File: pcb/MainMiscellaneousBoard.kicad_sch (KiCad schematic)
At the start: 1 part

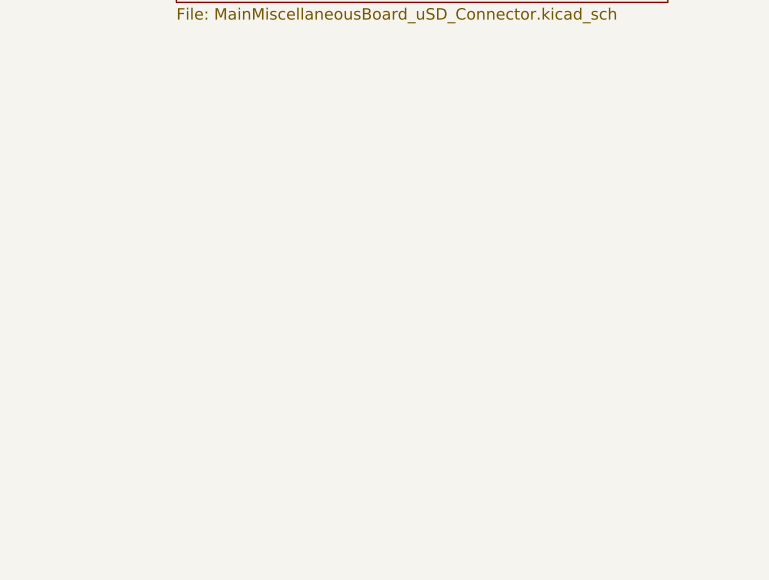
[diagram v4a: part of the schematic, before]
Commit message: Made symbol for ItsyBitsy ESP32.
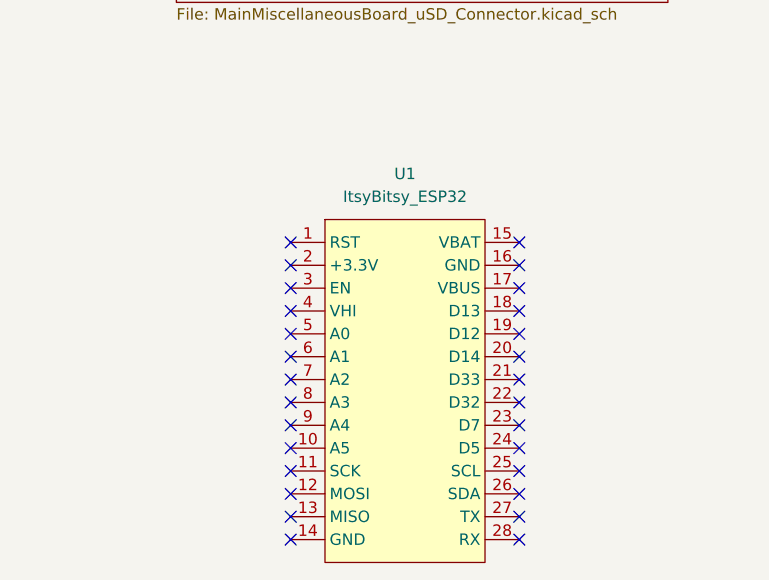
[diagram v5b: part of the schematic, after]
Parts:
- added U1: ItsyBitsy_ESP32, pcb:ItsyBitsy_ESP32, symbol ItsyBitsy_ESP32:ItsyBitsy_ESP32
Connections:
- no-connect marks 102 -> 130
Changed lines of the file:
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@@
 	(paper "A2")
 	(no_connect
+		(at 488.95 358.14)
+	)
+	(no_connect
+		(at 488.95 342.9)
+	)
+	(no_connect
 		(at 468.63 133.35)
 	)
@@
 	)
 	(no_connect
+		(at 514.35 340.36)
+	)
+	(no_connect
 		(at 468.63 166.37)
 	)
@@
 	)
 	(no_connect
+		(at 488.95 335.28)
+	)
+	(no_connect
 		(at 468.63 163.83)
 	)
@@
 	)
 	(no_connect
+		(at 514.35 353.06)
+	)
+	(no_connect
 		(at 468.63 105.41)
 	)
@@
 	)
 	(no_connect
+		(at 514.35 363.22)
+	)
+	(no_connect
+		(at 514.35 332.74)
+	)
+	(no_connect
 		(at 468.63 173.99)
 	)
@@
 	)
 	(no_connect
+		(at 514.35 350.52)
+	)
+	(no_connect
 		(at 468.63 143.51)
 	)
@@
 	)
 	(no_connect
+		(at 488.95 332.74)
+	)
+	(no_connect
 		(at 468.63 123.19)
 	)
@@
 	)
 	(no_connect
+		(at 514.35 355.6)
+	)
+	(no_connect
 		(at 468.63 72.39)
 	)
 	(no_connect
+		(at 514.35 345.44)
+	)
+	(no_connect
 		(at 468.63 87.63)
 	)
@@
 	)
 	(no_connect
+		(at 488.95 365.76)
+	)
+	(no_connect
 		(at 468.63 92.71)
 	)
@@
 	)
 	(no_connect
+		(at 514.35 335.28)
+	)
+	(no_connect
 		(at 537.21 125.73)
 	)
 	(no_connect
+		(at 488.95 353.06)
+	)
+	(no_connect
 		(at 537.21 82.55)
 	)
@@
 	)
 	(no_connect
+		(at 488.95 340.36)
+	)
+	(no_connect
+		(at 488.95 345.44)
+	)
+	(no_connect
 		(at 537.21 113.03)
 	)
 	(no_connect
+		(at 514.35 347.98)
+	)
+	(no_connect
 		(at 537.21 138.43)
 	)
@@
 	)
 	(no_connect
+		(at 514.35 358.14)
+	)
+	(no_connect
 		(at 468.63 77.47)
 	)
 	(no_connect
+		(at 514.35 342.9)
+	)
+	(no_connect
 		(at 468.63 85.09)
 	)
@@
 	)
 	(no_connect
+		(at 488.95 337.82)
+	)
+	(no_connect
 		(at 468.63 110.49)
 	)
@@
 	)
 	(no_connect
+		(at 514.35 337.82)
+	)
+	(no_connect
+		(at 488.95 363.22)
+	)
+	(no_connect
 		(at 537.21 95.25)
 	)
@@
 	)
 	(no_connect
+		(at 514.35 360.68)
+	)
+	(no_connect
+		(at 488.95 355.6)
+	)
+	(no_connect
 		(at 468.63 80.01)
 	)
@@
 	)
 	(no_connect
+		(at 488.95 350.52)
+	)
+	(no_connect
+		(at 514.35 365.76)
+	)
+	(no_connect
 		(at 537.21 156.21)
 	)
@@
 	)
 	(no_connect
+		(at 488.95 360.68)
+	)
+	(no_connect
 		(at 468.63 171.45)
 	)
@@
 	(no_connect
 		(at 537.21 118.11)
+	)
+	(no_connect
+		(at 488.95 347.98)
 	)
 	(no_connect
@@
 					(unit 1)
 				)
+			)
+		)
+	)
+	(symbol
+		(lib_id "ItsyBitsy_ESP32:ItsyBitsy_ESP32")
+		(at 501.65 330.2 0)
+		(unit 1)
+		(exclude_from_sim no)
+		(in_bom yes)
+		(on_board yes)
+		(dnp no)
+		(fields_autoplaced yes)
+		(property "Reference" "U1"
+			(at 501.65 325.12 0)
+			(effects
+				(font
+					(size 1.27 1.27)
+				)
+			)
+		)
+		(property "Value" "ItsyBitsy_ESP32"
+			(at 501.65 327.66 0)
+			(effects
+				(font
+					(size 1.27 1.27)
+				)
+			)
+		)
+		(property "Footprint" "pcb:ItsyBitsy_ESP32"
+			(at 501.65 330.2 0)
+			(effects
+				(font
+					(size 1.27 1.27)
+				)
+				(hide yes)
+			)
+		)
+		(property "Datasheet" ""
+			(at 501.65 330.2 0)
+			(effects
+				(font
+					(size 1.27 1.27)
+				)
+				(hide yes)
+			)
+		)
+		(property "Description" ""
+			(at 501.65 330.2 0)
+			(effects
+				(font
+					(size 1.27 1.27)
+				)
+				(hide yes)
+			)
+		)
+		(pin "1"
+		)
+		(pin "13"
+		)
+		(pin "7"
+		)
+		(pin "2"
+		)
+		(pin "6"
+		)
+		(pin "20"
+		)
+		(pin "4"
+		)
+		(pin "8"
+		)
+		(pin "10"
+		)
+		(pin "11"
+		)
+		(pin "3"
+		)
+		(pin "5"
+		)
+		(pin "9"
+		)
+		(pin "12"
+		)
+		(pin "15"
+		)
+		(pin "17"
+		)
+		(pin "18"
+		)
+		(pin "14"
+		)
+		(pin "16"
+		)
+		(pin "19"
+		)
+		(pin "24"
+		)
+		(pin "28"
+		)
+		(pin "21"
+		)
+		(pin "25"
+		)
+		(pin "26"
+		)
+		(pin "22"
+		)
+		(pin "27"
+		)
+		(pin "23"
+		)
+		(instances
+			(project ""
+				(path "/98fc9565-7d66-4cd3-b0d6-fc60566bea9b"
+					(reference "U1")
+					(unit 1)
+				)

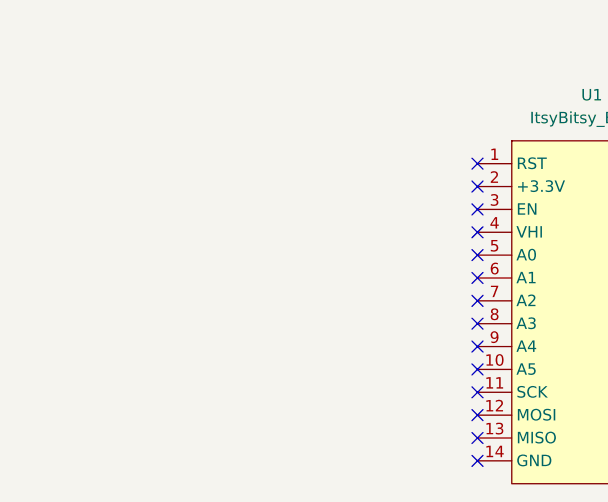
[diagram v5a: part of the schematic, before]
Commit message: Made SEEED Studio XIAO ESP32-S3 Sense symbol and footprint.
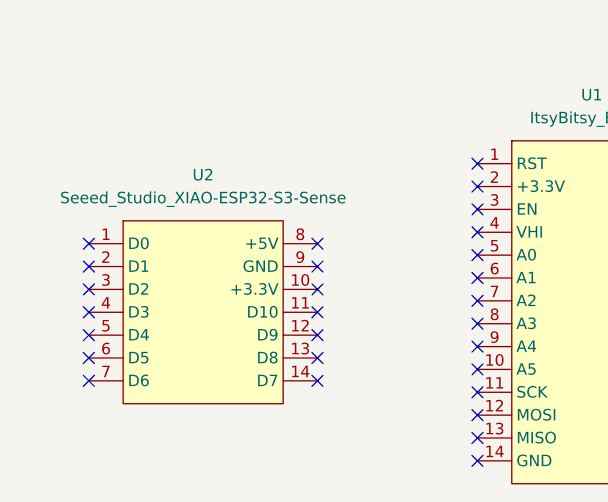
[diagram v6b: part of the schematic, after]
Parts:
- added U2: Seeed_Studio_XIAO-ESP32-S3-Sense, pcb:Seeed_Studio_XIAO_ESP32_S3, symbol Seeed_Studio_XIAO-ESP32-S3-Sense:Seeed_Studio_XIAO-ESP32-S3-Sense
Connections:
- no-connect marks 130 -> 144
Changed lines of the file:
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@@
 	(paper "A2")
 	(no_connect
+		(at 445.77 356.87)
+	)
+	(no_connect
 		(at 488.95 358.14)
 	)
@@
 	)
 	(no_connect
+		(at 471.17 346.71)
+	)
+	(no_connect
 		(at 468.63 166.37)
 	)
@@
 	)
 	(no_connect
+		(at 471.17 351.79)
+	)
+	(no_connect
 		(at 537.21 176.53)
 	)
@@
 	)
 	(no_connect
+		(at 471.17 341.63)
+	)
+	(no_connect
 		(at 468.63 95.25)
 	)
@@
 	)
 	(no_connect
+		(at 445.77 349.25)
+	)
+	(no_connect
 		(at 468.63 113.03)
 	)
@@
 	)
 	(no_connect
+		(at 445.77 341.63)
+	)
+	(no_connect
 		(at 468.63 128.27)
 	)
@@
 	)
 	(no_connect
+		(at 471.17 349.25)
+	)
+	(no_connect
 		(at 537.21 52.07)
 	)
 	(no_connect
+		(at 445.77 354.33)
+	)
+	(no_connect
 		(at 468.63 57.15)
 	)
@@
 	)
 	(no_connect
+		(at 445.77 351.79)
+	)
+	(no_connect
 		(at 537.21 82.55)
 	)
@@
 	)
 	(no_connect
+		(at 445.77 346.71)
+	)
+	(no_connect
 		(at 537.21 181.61)
 	)
@@
 	)
 	(no_connect
+		(at 445.77 344.17)
+	)
+	(no_connect
+		(at 471.17 356.87)
+	)
+	(no_connect
 		(at 488.95 345.44)
 	)
 	(no_connect
+		(at 471.17 344.17)
+	)
+	(no_connect
 		(at 537.21 113.03)
 	)
@@
 	(no_connect
 		(at 468.63 171.45)
+	)
+	(no_connect
+		(at 471.17 354.33)
 	)
 	(no_connect
@@
 					(unit 1)
 				)
+			)
+		)
+	)
+	(symbol
+		(lib_id "Seeed_Studio_XIAO-ESP32-S3-Sense:Seeed_Studio_XIAO-ESP32-S3-Sense")
+		(at 458.47 339.09 0)
+		(unit 1)
+		(exclude_from_sim no)
+		(in_bom yes)
+		(on_board yes)
+		(dnp no)
+		(fields_autoplaced yes)
+		(property "Reference" "U2"
+			(at 458.47 334.01 0)
+			(effects
+				(font
+					(size 1.27 1.27)
+				)
+			)
+		)
+		(property "Value" "Seeed_Studio_XIAO-ESP32-S3-Sense"
+			(at 458.47 336.55 0)
+			(effects
+				(font
+					(size 1.27 1.27)
+				)
+			)
+		)
+		(property "Footprint" "pcb:Seeed_Studio_XIAO_ESP32_S3"
+			(at 458.47 339.09 0)
+			(effects
+				(font
+					(size 1.27 1.27)
+				)
+				(hide yes)
+			)
+		)
+		(property "Datasheet" ""
+			(at 458.47 339.09 0)
+			(effects
+				(font
+					(size 1.27 1.27)
+				)
+				(hide yes)
+			)
+		)
+		(property "Description" ""
+			(at 458.47 339.09 0)
+			(effects
+				(font
+					(size 1.27 1.27)
+				)
+				(hide yes)
+			)
+		)
+		(pin "6"
+		)
+		(pin "13"
+		)
+		(pin "4"
+		)
+		(pin "9"
+		)
+		(pin "7"
+		)
+		(pin "5"
+		)
+		(pin "11"
+		)
+		(pin "8"
+		)
+		(pin "3"
+		)
+		(pin "10"
+		)
+		(pin "2"
+		)
+		(pin "1"
+		)
+		(pin "12"
+		)
+		(pin "14"
+		)
+		(instances
+			(project "MainMiscellaneousBoard"
+				(path "/98fc9565-7d66-4cd3-b0d6-fc60566bea9b"
+					(reference "U2")
+					(unit 1)
+				)

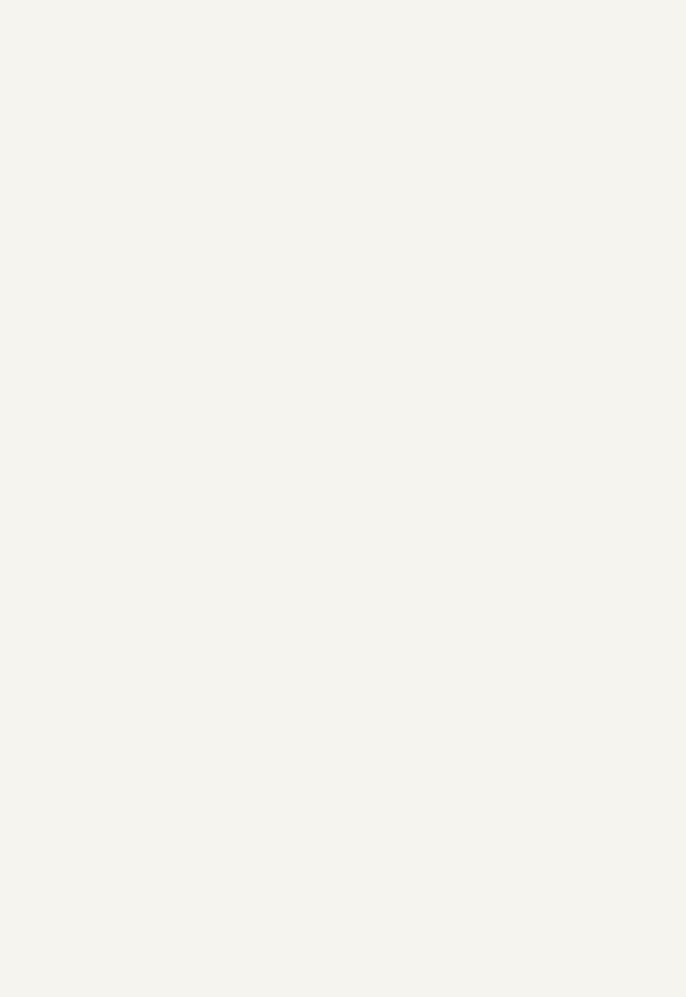
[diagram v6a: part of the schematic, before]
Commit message: Added in some miscellaneous connectors.
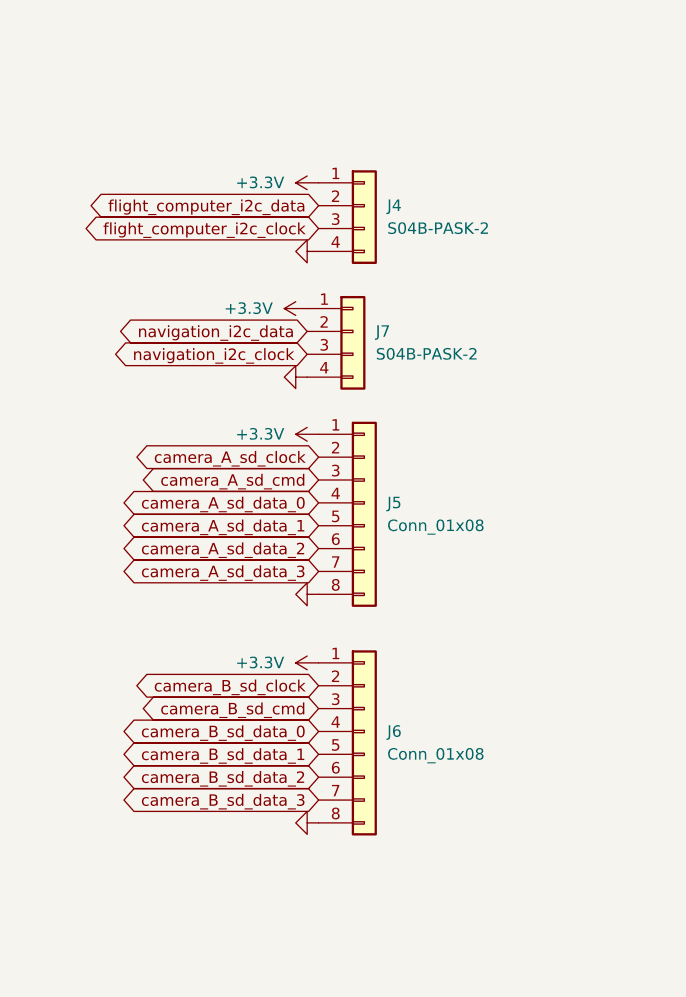
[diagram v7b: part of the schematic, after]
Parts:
- added J4, J7: S04B-PASK-2, pcb:S04B-PASK-2, symbol Connector_Generic:Conn_01x04
- added J5, J6: Conn_01x08, symbol Connector_Generic:Conn_01x08
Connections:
- net camera_A_sd_clock: now also J5.2 (Pin_2)
- net camera_A_sd_cmd: now also J5.3 (Pin_3)
- net camera_A_sd_data_0: now also J5.4 (Pin_4)
- net camera_A_sd_data_1: now also J5.5 (Pin_5)
- net camera_A_sd_data_2: now also J5.6 (Pin_6)
- net camera_A_sd_data_3: now also J5.7 (Pin_7)
- net camera_B_sd_clock: now also J6.2 (Pin_2)
- net camera_B_sd_cmd: now also J6.3 (Pin_3)
- net camera_B_sd_data_0: now also J6.4 (Pin_4)
- net camera_B_sd_data_1: now also J6.5 (Pin_5)
- net camera_B_sd_data_2: now also J6.6 (Pin_6)
- net camera_B_sd_data_3: now also J6.7 (Pin_7)
- new net +3.3V: J4.1 (Pin_1), J5.1 (Pin_1), J6.1 (Pin_1), J7.1 (Pin_1)
- new net GND: J4.4 (Pin_4), J5.8 (Pin_8), J6.8 (Pin_8), J7.4 (Pin_4)
- new net flight_computer_i2c_clock: J4.3 (Pin_3)
- new net flight_computer_i2c_data: J4.2 (Pin_2)
- new net navigation_i2c_clock: J7.3 (Pin_3)
- new net navigation_i2c_data: J7.2 (Pin_2)

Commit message: Added edge connector for `MainMiscellaneousBoard`.
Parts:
- removed J4, J7: S04B-PASK-2, pcb:S04B-PASK-2, symbol Connector_Generic:Conn_01x04
- removed J5, J6: Conn_01x08, symbol Connector_Generic:Conn_01x08
- added J8: PREC040DBAN-M71RC, Connector_PinHeader_2.54mm:PinHeader_2x16_P2.54mm_Horizontal, symbol Connector_Generic:Conn_02x16_Odd_Even
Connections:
- net +3.3V: now also J8.1 (Pin_1), J8.17 (Pin_17), J8.2 (Pin_2), J8.9 (Pin_9)
- net GND: now also J8.15 (Pin_15), J8.16 (Pin_16), J8.31 (Pin_31), J8.7 (Pin_7)
- net camera_A_sd_clock: now also J8.19 (Pin_19)
- net camera_A_sd_cmd: now also J8.21 (Pin_21)
- net camera_A_sd_data_0: now also J8.23 (Pin_23)
- net camera_A_sd_data_1: now also J8.25 (Pin_25)
- net camera_A_sd_data_2: now also J8.27 (Pin_27)
- net camera_A_sd_data_3: now also J8.29 (Pin_29)
- net camera_B_sd_clock: now also J8.4 (Pin_4)
- net camera_B_sd_cmd: now also J8.6 (Pin_6)
- net camera_B_sd_data_0: now also J8.8 (Pin_8)
- net camera_B_sd_data_1: now also J8.10 (Pin_10)
- net camera_B_sd_data_2: now also J8.12 (Pin_12)
- net camera_B_sd_data_3: now also J8.14 (Pin_14)
- net flight_computer_i2c_clock: now also J8.5 (Pin_5)
- net flight_computer_i2c_data: now also J8.3 (Pin_3)
- net navigation_i2c_clock: now also J8.13 (Pin_13)
- net navigation_i2c_data: now also J8.11 (Pin_11)
- no-connect marks 144 -> 152
